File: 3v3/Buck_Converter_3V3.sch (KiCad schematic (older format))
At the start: 10 parts, among them P1 CONN_2, P2 CONN_2, U1 LM2597

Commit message: updated to add a fuse and led
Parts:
- removed C1: 68uF, symbol C
- removed C4: 100uF, symbol C
- added C1: 68uF, symbol CP1
- added C4: 100uF, symbol CP1
- added D2: Power, symbol LED
- added F1: 500MA, symbol FUSE
- added P1: CONN_2, symbol CONN_2
- added R2: 100, symbol R
- D1: value DIODESCH -> HSMS-2800
- L1: value 100uH -> 300uH
- renumbered P1 to VIn1
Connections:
- net +12V: now also C1.1
- net +3.3V: now also F1.2, P1.1 (P1), R2.1; no longer L1.2, R1.1, U1.3 (VB), U1.4 (Feedback)
- net GND: now also C1.2, C4.2, D2.2 (K), P1.2 (PM)
- new net: D2.1 (A), R2.2
- new net Feedback: C4.1, F1.1, L1.2, R1.1, U1.3 (VB), U1.4 (Feedback)
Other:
- note added: "C1 must be:\n1.5x Max input voltage\nRMS curren rating > 200mA"
- note added: "D1 must be:\n1.5x max input V.\n1.3x max load current and/or equal to current limit of lm2597\nfast."
- moved on the sheet: P2, VIn1
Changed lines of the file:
@@
 Wire Wire Line
 	5350 4150 5350 4000
-$Comp
-L C C1
-U 1 1 538BA34A
-P 4300 3100
-F 0 "C1" H 4300 3200 40  0000 L CNN
-F 1 "68uF" H 4306 3015 40  0000 L CNN
-F 2 "" H 4338 2950 30  0000 C CNN
-F 3 "" H 4300 3100 60  0000 C CNN
-	1    4300 3100
-	1    0    0    -1
-$EndComp
 Wire Wire Line
 	3300 4050 5100 4050
@@
 P 6300 3600
 F 0 "D1" H 6300 3700 40  0000 C CNN
-F 1 "DIODESCH" H 6300 3500 40  0000 C CNN
+F 1 "HSMS-2800" H 6300 3500 40  0000 C CNN
 F 2 "" H 6300 3600 60  0000 C CNN
 F 3 "" H 6300 3600 60  0000 C CNN
@@
 P 6850 3400
 F 0 "L1" H 6850 3500 50  0000 C CNN
-F 1 "100uH" H 6850 3350 50  0000 C CNN
+F 1 "300uH" H 6850 3350 50  0000 C CNN
 F 2 "" H 6850 3400 60  0000 C CNN
 F 3 "" H 6850 3400 60  0000 C CNN
 	1    6850 3400
-	1    0    0    -1
-$EndComp
-$Comp
-L C C4
-U 1 1 538BA427
-P 7500 3700
-F 0 "C4" H 7500 3800 40  0000 L CNN
-F 1 "100uF" H 7506 3615 40  0000 L CNN
-F 2 "" H 7538 3550 30  0000 C CNN
-F 3 "" H 7500 3700 60  0000 C CNN
-	1    7500 3700
 	1    0    0    -1
 $EndComp
@@
 L +3.3V #PWR07
 U 1 1 538BA51E
-P 7950 3400
-F 0 "#PWR07" H 7950 3360 30  0001 C CNN
-F 1 "+3.3V" H 7950 3510 30  0000 C CNN
-F 2 "" H 7950 3400 60  0000 C CNN
-F 3 "" H 7950 3400 60  0000 C CNN
-	1    7950 3400
+P 8550 3350
+F 0 "#PWR07" H 8550 3310 30  0001 C CNN
+F 1 "+3.3V" H 8550 3460 30  0000 C CNN
+F 2 "" H 8550 3350 60  0000 C CNN
+F 3 "" H 8550 3350 60  0000 C CNN
+	1    8550 3350
 	1    0    0    -1
 $EndComp
@@
 L CONN_2 P2
 U 1 1 538CE314
-P 8650 4400
-F 0 "P2" V 8600 4400 40  0000 C CNN
-F 1 "CONN_2" V 8700 4400 40  0000 C CNN
-F 2 "" H 8650 4400 60  0000 C CNN
-F 3 "" H 8650 4400 60  0000 C CNN
-	1    8650 4400
-	1    0    0    -1
-$EndComp
-Wire Wire Line
-	8300 4300 8100 4300
-Wire Wire Line
-	8100 4300 8100 4200
-Wire Wire Line
-	8300 4500 8100 4500
-Wire Wire Line
-	8100 4500 8100 4600
-$Comp
-L CONN_2 P1
+P 8700 4750
+F 0 "P2" V 8650 4750 40  0000 C CNN
+F 1 "CONN_2" V 8750 4750 40  0000 C CNN
+F 2 "" H 8700 4750 60  0000 C CNN
+F 3 "" H 8700 4750 60  0000 C CNN
+	1    8700 4750
+	1    0    0    -1
+$EndComp
+Wire Wire Line
+	8350 4650 8150 4650
+Wire Wire Line
+	8150 4650 8150 4550
+Wire Wire Line
+	8350 4850 8150 4850
+Wire Wire Line
+	8150 4850 8150 4950
+$Comp
+L CONN_2 VIn1
 U 1 1 538CE366
-P 8600 5200
-F 0 "P1" V 8550 5200 40  0000 C CNN
-F 1 "CONN_2" V 8650 5200 40  0000 C CNN
-F 2 "" H 8600 5200 60  0000 C CNN
-F 3 "" H 8600 5200 60  0000 C CNN
-	1    8600 5200
-	1    0    0    -1
-$EndComp
-Wire Wire Line
-	8250 5100 8100 5100
-Wire Wire Line
-	8100 5100 8100 5000
-Wire Wire Line
-	8250 5300 8100 5300
-Wire Wire Line
-	8100 5300 8100 5350
+P 8650 5550
+F 0 "VIn1" V 8600 5550 40  0000 C CNN
+F 1 "CONN_2" V 8700 5550 40  0000 C CNN
+F 2 "" H 8650 5550 60  0000 C CNN
+F 3 "" H 8650 5550 60  0000 C CNN
+	1    8650 5550
+	1    0    0    -1
+$EndComp
+Wire Wire Line
+	8300 5450 8150 5450
+Wire Wire Line
+	8150 5450 8150 5350
+Wire Wire Line
+	8300 5650 8150 5650
+Wire Wire Line
+	8150 5650 8150 5700
 $Comp
 L GND #PWR09
 U 1 1 538CE3C0
-P 8100 4600
-F 0 "#PWR09" H 8100 4600 30  0001 C CNN
-F 1 "GND" H 8100 4530 30  0001 C CNN
-F 2 "" H 8100 4600 60  0000 C CNN
-F 3 "" H 8100 4600 60  0000 C CNN
-	1    8100 4600
+P 8150 4950
+F 0 "#PWR09" H 8150 4950 30  0001 C CNN
+F 1 "GND" H 8150 4880 30  0001 C CNN
+F 2 "" H 8150 4950 60  0000 C CNN
+F 3 "" H 8150 4950 60  0000 C CNN
+	1    8150 4950
 	1    0    0    -1
 $EndComp
@@
 L GND #PWR010
 U 1 1 538CE3D4
-P 8100 5350
-F 0 "#PWR010" H 8100 5350 30  0001 C CNN
-F 1 "GND" H 8100 5280 30  0001 C CNN
-F 2 "" H 8100 5350 60  0000 C CNN
-F 3 "" H 8100 5350 60  0000 C CNN
-	1    8100 5350
+P 8150 5700
+F 0 "#PWR010" H 8150 5700 30  0001 C CNN
+F 1 "GND" H 8150 5630 30  0001 C CNN
+F 2 "" H 8150 5700 60  0000 C CNN
+F 3 "" H 8150 5700 60  0000 C CNN
+	1    8150 5700
 	1    0    0    -1
 $EndComp
@@
 L +3.3V #PWR011
 U 1 1 538CE3E8
-P 8100 4200
-F 0 "#PWR011" H 8100 4160 30  0001 C CNN
-F 1 "+3.3V" H 8100 4310 30  0000 C CNN
-F 2 "" H 8100 4200 60  0000 C CNN
-F 3 "" H 8100 4200 60  0000 C CNN
-	1    8100 4200
+P 8150 4550
+F 0 "#PWR011" H 8150 4510 30  0001 C CNN
+F 1 "+3.3V" H 8150 4660 30  0000 C CNN
+F 2 "" H 8150 4550 60  0000 C CNN
+F 3 "" H 8150 4550 60  0000 C CNN
+	1    8150 4550
 	1    0    0    -1
 $EndComp
@@
 L +12V #PWR012
 U 1 1 538CE3FC
-P 8100 5000
-F 0 "#PWR012" H 8100 4950 20  0001 C CNN
-F 1 "+12V" H 8100 5100 30  0000 C CNN
-F 2 "" H 8100 5000 60  0000 C CNN
-F 3 "" H 8100 5000 60  0000 C CNN
-	1    8100 5000
+P 8150 5350
+F 0 "#PWR012" H 8150 5300 20  0001 C CNN
+F 1 "+12V" H 8150 5450 30  0000 C CNN
+F 2 "" H 8150 5350 60  0000 C CNN
+F 3 "" H 8150 5350 60  0000 C CNN
+	1    8150 5350
 	1    0    0    -1
 $EndComp
@@
 	-1   0    0    1
 $EndComp
+Text Notes 1600 5650 0    60   ~ 0
+D1 must be:\n1.5x max input V.\n1.3x max load current and/or equal to current limit of lm2597\nfast.
+Text Notes 1600 5150 0    60   ~ 0
+C1 must be:\n1.5x Max input voltage\nRMS curren rating > 200mA
+$Comp
+L R R2
+U 1 1 53A3524C
+P 9050 2850
+F 0 "R2" V 9130 2850 40  0000 C CNN
+F 1 "100" V 9057 2851 40  0000 C CNN
+F 2 "" V 8980 2850 30  0000 C CNN
+F 3 "" H 9050 2850 30  0000 C CNN
+	1    9050 2850
+	1    0    0    -1
+$EndComp
+$Comp
+L LED D2
+U 1 1 53A35290
+P 9050 3400
+F 0 "D2" H 9050 3500 50  0000 C CNN
+F 1 "Power" H 9050 3300 50  0000 C CNN
+F 2 "" H 9050 3400 60  0000 C CNN
+F 3 "" H 9050 3400 60  0000 C CNN
+	1    9050 3400
+	0    1    1    0
+$EndComp
+Wire Wire Line
+	9050 3200 9050 3100
+$Comp
+L +3.3V #PWR019
+U 1 1 53A352CD
+P 9050 2500
+F 0 "#PWR019" H 9050 2460 30  0001 C CNN
+F 1 "+3.3V" H 9050 2610 30  0000 C CNN
+F 2 "" H 9050 2500 60  0000 C CNN
+F 3 "" H 9050 2500 60  0000 C CNN
+	1    9050 2500
+	1    0    0    -1
+$EndComp
+$Comp
+L GND #PWR020
+U 1 1 53A352E1
+P 9050 3700
+F 0 "#PWR020" H 9050 3700 30  0001 C CNN
+F 1 "GND" H 9050 3630 30  0001 C CNN
+F 2 "" H 9050 3700 60  0000 C CNN
+F 3 "" H 9050 3700 60  0000 C CNN
+	1    9050 3700
+	1    0    0    -1
+$EndComp
+Wire Wire Line
+	9050 2600 9050 2500
+Wire Wire Line
+	9050 3700 9050 3600
+$Comp
+L FUSE F1
+U 1 1 53A35354
+P 8200 3400
+F 0 "F1" H 8300 3450 40  0000 C CNN
+F 1 "500MA" H 8100 3350 40  0000 C CNN
+F 2 "" H 8200 3400 60  0000 C CNN
+F 3 "" H 8200 3400 60  0000 C CNN
+	1    8200 3400
+	1    0    0    -1
+$EndComp
+Wire Wire Line
+	8450 3400 8550 3400
+Wire Wire Line
+	8550 3400 8550 3350
+$Comp
+L CP1 C4
+U 1 1 53A353B5
+P 7500 3700
+F 0 "C4" H 7550 3800 50  0000 L CNN
+F 1 "100uF" H 7550 3600 50  0000 L CNN
+F 2 "" H 7500 3700 60  0000 C CNN
+F 3 "" H 7500 3700 60  0000 C CNN
+	1    7500 3700
+	1    0    0    -1
+$EndComp
+$Comp
+L CP1 C1
+U 1 1 53A353C9
+P 4300 3100
+F 0 "C1" H 4350 3200 50  0000 L CNN
+F 1 "68uF" H 4350 3000 50  0000 L CNN
+F 2 "" H 4300 3100 60  0000 C CNN
+F 3 "" H 4300 3100 60  0000 C CNN
+	1    4300 3100
+	1    0    0    -1
+$EndComp
+$Comp
+L CONN_2 P1
+U 1 1 53A3D2AB
+P 9650 4750
+F 0 "P1" V 9600 4750 40  0000 C CNN
+F 1 "CONN_2" V 9700 4750 40  0000 C CNN
+F 2 "" H 9650 4750 60  0000 C CNN
+F 3 "" H 9650 4750 60  0000 C CNN
+	1    9650 4750
+	1    0    0    -1
+$EndComp
+Wire Wire Line
+	9300 4650 9100 4650
+Wire Wire Line
+	9100 4650 9100 4550
+Wire Wire Line
+	9300 4850 9100 4850
+Wire Wire Line
+	9100 4850 9100 4950
+$Comp
+L GND #PWR021
+U 1 1 53A3D2B5
+P 9100 4950
+F 0 "#PWR021" H 9100 4950 30  0001 C CNN
+F 1 "GND" H 9100 4880 30  0001 C CNN
+F 2 "" H 9100 4950 60  0000 C CNN
+F 3 "" H 9100 4950 60  0000 C CNN
+	1    9100 4950
+	1    0    0    -1
+$EndComp
+$Comp
+L +3.3V #PWR022
+U 1 1 53A3D2BB
+P 9100 4550
+F 0 "#PWR022" H 9100 4510 30  0001 C CNN
+F 1 "+3.3V" H 9100 4660 30  0000 C CNN
+F 2 "" H 9100 4550 60  0000 C CNN
+F 3 "" H 9100 4550 60  0000 C CNN
+	1    9100 4550
+	1    0    0    -1
+$EndComp
 $EndSCHEMATC

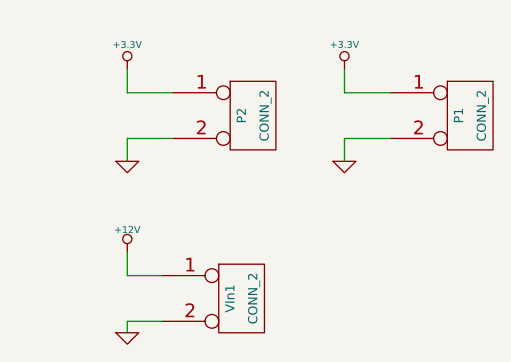
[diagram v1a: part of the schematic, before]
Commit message: Added additional pin input
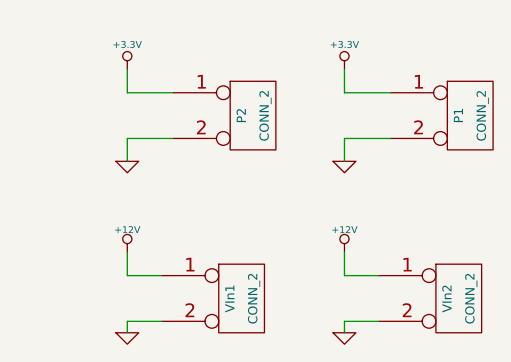
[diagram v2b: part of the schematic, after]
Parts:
- added VIn2: CONN_2, symbol CONN_2
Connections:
- net +12V: now also VIn2.1 (P1)
- net GND: now also VIn2.2 (PM)
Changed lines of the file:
@@
 	5600 4000 5600 4650
 $Comp
-L GND #PWR01
+L GND #PWR2
 U 1 1 538BA3AF
 P 4300 3400
-F 0 "#PWR01" H 4300 3400 30  0001 C CNN
+F 0 "#PWR2" H 4300 3400 30  0001 C CNN
 F 1 "GND" H 4300 3330 30  0001 C CNN
 F 2 "" H 4300 3400 60  0000 C CNN
@@
 $EndComp
 $Comp
-L GND #PWR02
+L GND #PWR3
 U 1 1 538BA3C3
 P 5100 4650
-F 0 "#PWR02" H 5100 4650 30  0001 C CNN
+F 0 "#PWR3" H 5100 4650 30  0001 C CNN
 F 1 "GND" H 5100 4580 30  0001 C CNN
 F 2 "" H 5100 4650 60  0000 C CNN
@@
 $EndComp
 $Comp
-L GND #PWR03
+L GND #PWR4
 U 1 1 538BA3D7
 P 5350 4650
-F 0 "#PWR03" H 5350 4650 30  0001 C CNN
+F 0 "#PWR4" H 5350 4650 30  0001 C CNN
 F 1 "GND" H 5350 4580 30  0001 C CNN
 F 2 "" H 5350 4650 60  0000 C CNN
@@
 $EndComp
 $Comp
-L GND #PWR04
+L GND #PWR5
 U 1 1 538BA3EB
 P 5600 4650
-F 0 "#PWR04" H 5600 4650 30  0001 C CNN
+F 0 "#PWR5" H 5600 4650 30  0001 C CNN
 F 1 "GND" H 5600 4580 30  0001 C CNN
 F 2 "" H 5600 4650 60  0000 C CNN
@@
 $EndComp
 $Comp
-L GND #PWR05
+L GND #PWR10
 U 1 1 538BA43B
 P 7500 4050
-F 0 "#PWR05" H 7500 4050 30  0001 C CNN
+F 0 "#PWR10" H 7500 4050 30  0001 C CNN
 F 1 "GND" H 7500 3980 30  0001 C CNN
 F 2 "" H 7500 4050 60  0000 C CNN
@@
 	7500 4050 7500 3900
 $Comp
-L GND #PWR06
+L GND #PWR6
 U 1 1 538BA4AD
 P 6300 4050
-F 0 "#PWR06" H 6300 4050 30  0001 C CNN
+F 0 "#PWR6" H 6300 4050 30  0001 C CNN
 F 1 "GND" H 6300 3980 30  0001 C CNN
 F 2 "" H 6300 4050 60  0000 C CNN
@@
 Connection ~ 7500 3250
 $Comp
-L +3.3V #PWR07
+L +3.3V #PWR15
 U 1 1 538BA51E
 P 8550 3350
-F 0 "#PWR07" H 8550 3310 30  0001 C CNN
+F 0 "#PWR15" H 8550 3310 30  0001 C CNN
 F 1 "+3.3V" H 8550 3460 30  0000 C CNN
 F 2 "" H 8550 3350 60  0000 C CNN
@@
 $EndComp
 $Comp
-L +12V #PWR08
+L +12V #PWR1
 U 1 1 538BA532
 P 4300 2850
-F 0 "#PWR08" H 4300 2800 20  0001 C CNN
+F 0 "#PWR1" H 4300 2800 20  0001 C CNN
 F 1 "+12V" H 4300 2950 30  0000 C CNN
 F 2 "" H 4300 2850 60  0000 C CNN
@@
 	8150 5650 8150 5700
 $Comp
-L GND #PWR09
+L GND #PWR12
 U 1 1 538CE3C0
 P 8150 4950
-F 0 "#PWR09" H 8150 4950 30  0001 C CNN
+F 0 "#PWR12" H 8150 4950 30  0001 C CNN
 F 1 "GND" H 8150 4880 30  0001 C CNN
 F 2 "" H 8150 4950 60  0000 C CNN
@@
 $EndComp
 $Comp
-L GND #PWR010
+L GND #PWR14
 U 1 1 538CE3D4
 P 8150 5700
-F 0 "#PWR010" H 8150 5700 30  0001 C CNN
+F 0 "#PWR14" H 8150 5700 30  0001 C CNN
 F 1 "GND" H 8150 5630 30  0001 C CNN
 F 2 "" H 8150 5700 60  0000 C CNN
@@
 $EndComp
 $Comp
-L +3.3V #PWR011
+L +3.3V #PWR11
 U 1 1 538CE3E8
 P 8150 4550
-F 0 "#PWR011" H 8150 4510 30  0001 C CNN
+F 0 "#PWR11" H 8150 4510 30  0001 C CNN
 F 1 "+3.3V" H 8150 4660 30  0000 C CNN
 F 2 "" H 8150 4550 60  0000 C CNN
@@
 $EndComp
 $Comp
-L +12V #PWR012
+L +12V #PWR13
 U 1 1 538CE3FC
 P 8150 5350
-F 0 "#PWR012" H 8150 5300 20  0001 C CNN
+F 0 "#PWR13" H 8150 5300 20  0001 C CNN
 F 1 "+12V" H 8150 5450 30  0000 C CNN
 F 2 "" H 8150 5350 60  0000 C CNN
@@
 $EndComp
 $Comp
-L PWR_FLAG #FLG013
+L PWR_FLAG #FLG3
 U 1 1 538CE447
 P 7450 5050
-F 0 "#FLG013" H 7450 5145 30  0001 C CNN
+F 0 "#FLG3" H 7450 5145 30  0001 C CNN
 F 1 "PWR_FLAG" H 7450 5230 30  0000 C CNN
 F 2 "" H 7450 5050 60  0000 C CNN
@@
 $EndComp
 $Comp
-L +12V #PWR014
+L +12V #PWR9
 U 1 1 538CE45B
 P 7450 5150
-F 0 "#PWR014" H 7450 5100 20  0001 C CNN
+F 0 "#PWR9" H 7450 5100 20  0001 C CNN
 F 1 "+12V" H 7450 5250 30  0000 C CNN
 F 2 "" H 7450 5150 60  0000 C CNN
@@
 	7450 5150 7450 5050
 $Comp
-L PWR_FLAG #FLG015
+L PWR_FLAG #FLG2
 U 1 1 538CE497
 P 7150 5050
-F 0 "#FLG015" H 7150 5145 30  0001 C CNN
+F 0 "#FLG2" H 7150 5145 30  0001 C CNN
 F 1 "PWR_FLAG" H 7150 5230 30  0000 C CNN
 F 2 "" H 7150 5050 60  0000 C CNN
@@
 $EndComp
 $Comp
-L GND #PWR016
+L GND #PWR8
 U 1 1 538CE4AB
 P 7150 5150
-F 0 "#PWR016" H 7150 5150 30  0001 C CNN
+F 0 "#PWR8" H 7150 5150 30  0001 C CNN
 F 1 "GND" H 7150 5080 30  0001 C CNN
 F 2 "" H 7150 5150 60  0000 C CNN
@@
 	7150 5050 7150 5150
 $Comp
-L PWR_FLAG #FLG017
+L PWR_FLAG #FLG1
 U 1 1 538CE4F2
 P 6850 5050
-F 0 "#FLG017" H 6850 5145 30  0001 C CNN
+F 0 "#FLG1" H 6850 5145 30  0001 C CNN
 F 1 "PWR_FLAG" H 6850 5230 30  0000 C CNN
 F 2 "" H 6850 5050 60  0000 C CNN
@@
 	6850 5050 6850 5150
 $Comp
-L +3.3V #PWR018
+L +3.3V #PWR7
 U 1 1 538CE52E
 P 6850 5150
-F 0 "#PWR018" H 6850 5110 30  0001 C CNN
+F 0 "#PWR7" H 6850 5110 30  0001 C CNN
 F 1 "+3.3V" H 6850 5260 30  0000 C CNN
 F 2 "" H 6850 5150 60  0000 C CNN
@@
 	9050 3200 9050 3100
 $Comp
-L +3.3V #PWR019
+L +3.3V #PWR16
 U 1 1 53A352CD
 P 9050 2500
-F 0 "#PWR019" H 9050 2460 30  0001 C CNN
+F 0 "#PWR16" H 9050 2460 30  0001 C CNN
 F 1 "+3.3V" H 9050 2610 30  0000 C CNN
 F 2 "" H 9050 2500 60  0000 C CNN
@@
 $EndComp
 $Comp
-L GND #PWR020
+L GND #PWR17
 U 1 1 53A352E1
 P 9050 3700
-F 0 "#PWR020" H 9050 3700 30  0001 C CNN
+F 0 "#PWR17" H 9050 3700 30  0001 C CNN
 F 1 "GND" H 9050 3630 30  0001 C CNN
 F 2 "" H 9050 3700 60  0000 C CNN
@@
 	9100 4850 9100 4950
 $Comp
-L GND #PWR021
+L GND #PWR19
 U 1 1 53A3D2B5
 P 9100 4950
-F 0 "#PWR021" H 9100 4950 30  0001 C CNN
+F 0 "#PWR19" H 9100 4950 30  0001 C CNN
 F 1 "GND" H 9100 4880 30  0001 C CNN
 F 2 "" H 9100 4950 60  0000 C CNN
@@
 $EndComp
 $Comp
-L +3.3V #PWR022
+L +3.3V #PWR18
 U 1 1 53A3D2BB
 P 9100 4550
-F 0 "#PWR022" H 9100 4510 30  0001 C CNN
+F 0 "#PWR18" H 9100 4510 30  0001 C CNN
 F 1 "+3.3V" H 9100 4660 30  0000 C CNN
 F 2 "" H 9100 4550 60  0000 C CNN
@@
 	1    0    0    -1
 $EndComp
+$Comp
+L CONN_2 VIn2
+U 1 1 53C5B357
+P 9600 5550
+F 0 "VIn2" V 9550 5550 40  0000 C CNN
+F 1 "CONN_2" V 9650 5550 40  0000 C CNN
+F 2 "" H 9600 5550 60  0000 C CNN
+F 3 "" H 9600 5550 60  0000 C CNN
+	1    9600 5550
+	1    0    0    -1
+$EndComp
+Wire Wire Line
+	9250 5450 9100 5450
+Wire Wire Line
+	9100 5450 9100 5350
+Wire Wire Line
+	9250 5650 9100 5650
+Wire Wire Line
+	9100 5650 9100 5700
+$Comp
+L GND #PWR21
+U 1 1 53C5B361
+P 9100 5700
+F 0 "#PWR21" H 9100 5700 30  0001 C CNN
+F 1 "GND" H 9100 5630 30  0001 C CNN
+F 2 "" H 9100 5700 60  0000 C CNN
+F 3 "" H 9100 5700 60  0000 C CNN
+	1    9100 5700
+	1    0    0    -1
+$EndComp
+$Comp
+L +12V #PWR20
+U 1 1 53C5B367
+P 9100 5350
+F 0 "#PWR20" H 9100 5300 20  0001 C CNN
+F 1 "+12V" H 9100 5450 30  0000 C CNN
+F 2 "" H 9100 5350 60  0000 C CNN
+F 3 "" H 9100 5350 60  0000 C CNN
+	1    9100 5350
+	1    0    0    -1
+$EndComp
